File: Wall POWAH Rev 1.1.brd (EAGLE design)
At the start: 36.8 x 53.3 mm, 13 parts

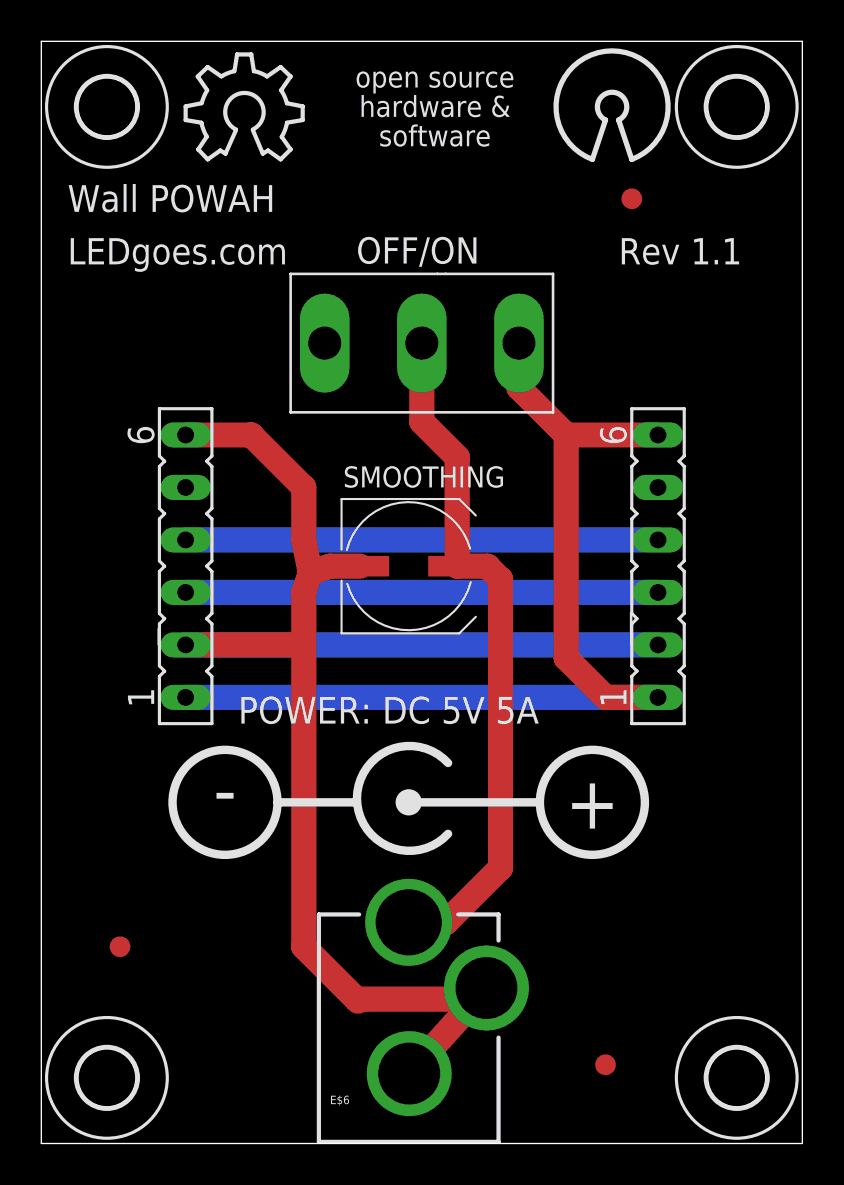
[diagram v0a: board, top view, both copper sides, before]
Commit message: Slight changes made to Rev 1 before production, including Power LED and polarity silkscreening
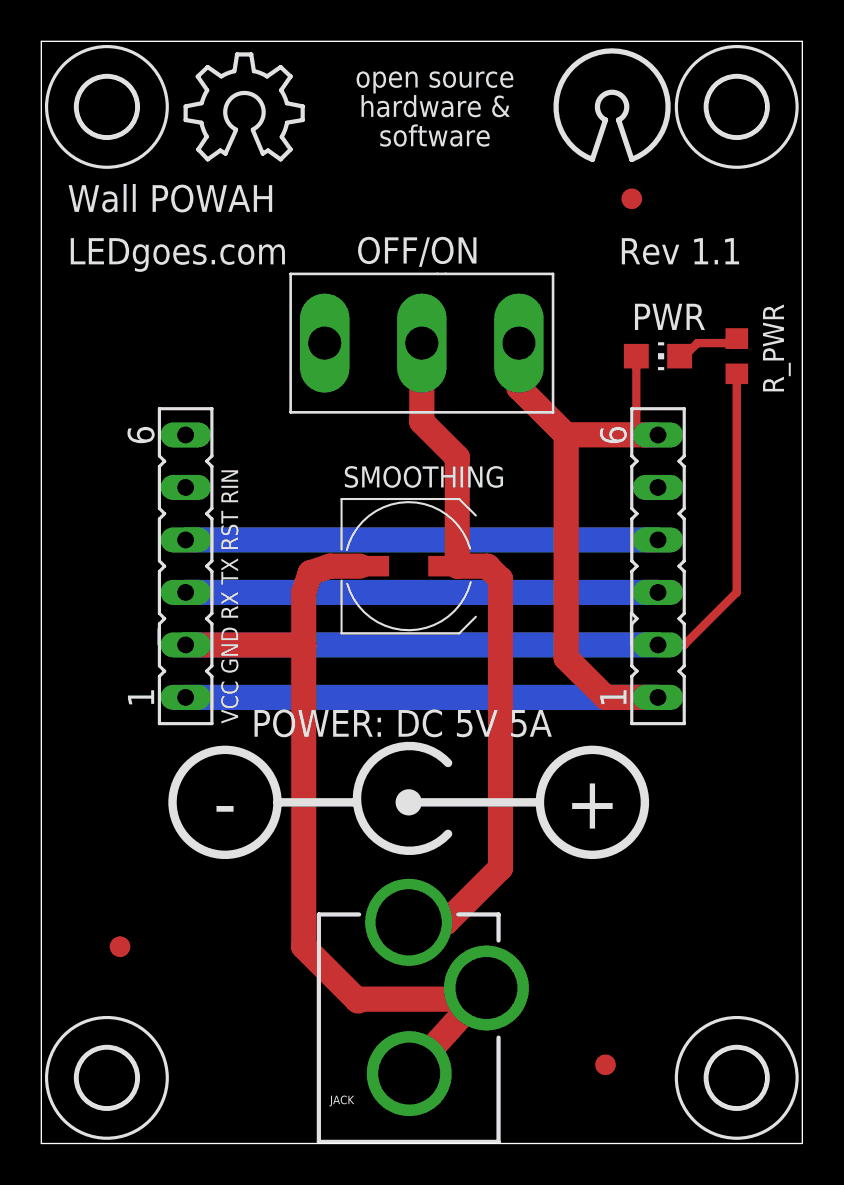
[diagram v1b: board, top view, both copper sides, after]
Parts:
- added PWR: (no value), led:CHIP-LED0805
- added R_PWR: (no value), eagle-ltspice:R0603
- renumbered E$6 to JACK
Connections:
- new net S$5: PWR.C, R_PWR.2
- net GND: now also R_PWR.1; no longer _.6
- net VCC: now also PWR.A
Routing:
- net GND: track 75.9 -> 80.5 mm
- net VCC: track 48.7 -> 52.7 mm
- net S$5: track 0.00 -> 3.11 mm
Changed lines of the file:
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@@
 <wire x1="43.18" y1="50.8" x2="6.35" y2="50.8" width="0" layer="20"/>
 <text x="7.62" y="40.005" size="1.27" layer="25" font="vector">LEDgoes.com</text>
-<text x="10.16" y="17.78" size="0.8128" layer="26" font="vector" rot="MR90">VCC GND RX TX RST RIN</text>
+<text x="15.875" y="17.78" size="0.8128" layer="25" font="vector" rot="R90">VCC GND RX TX RST RIN</text>
 <text x="25.4" y="45.72" size="1.016" layer="25" font="vector" distance="40" align="bottom-center">open source
 hardware &amp;
@@
 <text x="7.62" y="42.545" size="1.2954" layer="25" font="vector">Wall POWAH</text>
 <text x="34.29" y="40.005" size="1.27" layer="25" font="vector">Rev 1.1</text>
-<text x="15.875" y="17.78" size="1.2954" layer="25" font="vector">POWER: DC 5V 5A</text>
+<text x="16.51" y="17.145" size="1.2954" layer="25" font="vector">POWER: DC 5V 5A</text>
 <circle x="15.24" y="13.97" radius="2.54" width="0.4064" layer="25"/>
 <wire x1="26.035" y1="12.446" x2="26.035" y2="15.875" width="0.4064" layer="25" curve="-275"/>
@@
 <circle x="24.13" y="13.97" radius="0.635" width="0" layer="25"/>
 <wire x1="24.765" y1="13.97" x2="30.48" y2="13.97" width="0.4064" layer="25"/>
-<text x="15.24" y="13.335" size="2.54" layer="25" align="bottom-center">-</text>
-<text x="33.02" y="12.7" size="2.54" layer="25" align="bottom-center">+</text>
+<text x="15.24" y="12.7" size="2.54" layer="25" font="vector" align="bottom-center">-</text>
+<text x="33.02" y="12.7" size="2.54" layer="25" font="vector" align="bottom-center">+</text>
 </plain>
 <attributes>
@@
 <element name="E$2" library="holes" package="2,8" value="" x="40.005" y="47.625"/>
 <element name="E$5" library="holes" package="2,8" value="" x="40.005" y="0.635"/>
-<element name="E$6" library="SparkFun-Connectors" package="POWER_JACK_PTH_LOCK" value="" x="24.13" y="-5.715"/>
-<element name="SMOOTHING" library="rcl" package="UD-6,3X7,7_NICHICON" value="100uF" x="24.13" y="25.4"/>
+<element name="JACK" library="SparkFun-Connectors" package="POWER_JACK_PTH_LOCK" value="" x="24.13" y="-5.715"/>
+<element name="SMOOTHING" library="rcl" package="UD-6,3X7,7_NICHICON" value="100uF" x="24.13" y="25.4" smashed="yes">
+<attribute name="NAME" x="20.955" y="29.21" size="1.016" layer="25" font="vector"/>
+<attribute name="VALUE" x="20.955" y="20.955" size="1.016" layer="27" font="vector"/>
+</element>
 <element name="OFF/ON" library="LEDgoes" package="SPDT-5A" value=" " x="24.765" y="36.195" smashed="yes">
-<attribute name="NAME" x="21.59" y="40.045" size="1.27" layer="25"/>
+<attribute name="NAME" x="21.59" y="40.045" size="1.27" layer="25" font="vector"/>
 </element>
 <element name="E$7" library="adafruit" package="FIDUCIAL_1MM" value="" x="34.925" y="43.18"/>
 <element name="E$8" library="adafruit" package="FIDUCIAL_1MM" value="" x="33.655" y="1.27"/>
 <element name="E$9" library="adafruit" package="FIDUCIAL_1MM" value="" x="10.16" y="6.985"/>
+<element name="PWR" library="led" package="CHIP-LED0805" value="" x="36.195" y="35.56" smashed="yes" rot="R270">
+<attribute name="NAME" x="34.925" y="36.83" size="1.27" layer="25" font="vector"/>
+<attribute name="VALUE" x="34.925" y="33.02" size="1.27" layer="27"/>
+</element>
+<element name="R_PWR" library="eagle-ltspice" package="R0603" value="" x="40.005" y="35.56" smashed="yes" rot="R90">
+<attribute name="NAME" x="41.275" y="38.1" size="1.016" layer="25" font="vector" rot="R270"/>
+<attribute name="VALUE" x="41.91" y="34.925" size="1.27" layer="27" rot="R90"/>
+</element>
 </elements>
 <signals>
@@
 <wire x1="19.3675" y1="25.0825" x2="20.32" y2="25.4" width="1.2192" layer="1"/>
 <wire x1="20.32" y1="25.4" x2="21.78" y2="25.4" width="1.2192" layer="1"/>
-<contactref element="E$6" pad="GNDBREAK"/>
-<contactref element="E$6" pad="GND"/>
+<contactref element="JACK" pad="GNDBREAK"/>
+<contactref element="JACK" pad="GND"/>
 <wire x1="24.1554" y1="0.842" x2="27.8916" y2="4.985" width="1.2192" layer="1"/>
 <wire x1="27.8916" y1="4.985" x2="27.845" y2="4.985" width="1.2192" layer="1"/>
 <wire x1="27.845" y1="4.985" x2="27.305" y2="4.445" width="1.2192" layer="1"/>
 <wire x1="27.305" y1="4.445" x2="21.59" y2="4.445" width="1.2192" layer="1"/>
-<contactref element="_" pad="6"/>
-<wire x1="13.335" y1="31.75" x2="16.51" y2="31.75" width="1.2192" layer="1"/>
-<wire x1="16.51" y1="31.75" x2="19.05" y2="29.21" width="1.2192" layer="1"/>
-<wire x1="19.05" y1="29.21" x2="19.05" y2="26.67" width="1.2192" layer="1"/>
-<wire x1="19.05" y1="26.67" x2="19.3675" y2="25.0825" width="1.2192" layer="1"/>
+<contactref element="R_PWR" pad="1"/>
+<wire x1="40.005" y1="34.71" x2="40.005" y2="24.13" width="0.4064" layer="1"/>
+<wire x1="40.005" y1="24.13" x2="37.465" y2="21.59" width="0.4064" layer="1"/>
+<wire x1="37.465" y1="21.59" x2="36.195" y2="21.59" width="0.4064" layer="1"/>
 </signal>
 <signal name="VCC">
@@
 <wire x1="29.465" y1="36.195" x2="29.465" y2="34.035" width="1.2192" layer="1"/>
 <wire x1="29.465" y1="34.035" x2="31.75" y2="31.75" width="1.2192" layer="1"/>
-<wire x1="31.75" y1="31.75" x2="36.195" y2="31.75" width="1.2192" layer="1"/>
+<wire x1="31.75" y1="31.75" x2="35.56" y2="31.75" width="1.2192" layer="1"/>
+<wire x1="35.56" y1="31.75" x2="36.195" y2="31.75" width="1.2192" layer="1"/>
 <wire x1="36.195" y1="19.05" x2="33.655" y2="19.05" width="1.2192" layer="1"/>
 <wire x1="33.655" y1="19.05" x2="31.75" y2="20.955" width="1.2192" layer="1"/>
 <wire x1="31.75" y1="20.955" x2="31.75" y2="31.75" width="1.2192" layer="1"/>
+<contactref element="PWR" pad="A"/>
+<wire x1="35.145" y1="35.56" x2="35.145" y2="32.165" width="0.4064" layer="1"/>
+<wire x1="35.145" y1="32.165" x2="35.56" y2="31.75" width="0.4064" layer="1"/>
 </signal>
 <signal name="S$1">
 <contactref element="SMOOTHING" pad="+"/>
-<contactref element="E$6" pad="PWR"/>
+<contactref element="JACK" pad="PWR"/>
 <wire x1="24.13" y1="8.1628" x2="25.9428" y2="8.1628" width="1.2192" layer="1"/>
 <wire x1="25.9428" y1="8.1628" x2="28.575" y2="10.795" width="1.2192" layer="1"/>
@@
 <wire x1="36.195" y1="26.67" x2="13.335" y2="26.67" width="1.2192" layer="16"/>
 </signal>
+<signal name="S$5">
+<contactref element="R_PWR" pad="2"/>
+<contactref element="PWR" pad="C"/>
+<wire x1="37.245" y1="35.56" x2="37.465" y2="35.56" width="0.4064" layer="1"/>
+<wire x1="37.465" y1="35.56" x2="38.1" y2="36.195" width="0.4064" layer="1"/>
+<wire x1="38.1" y1="36.195" x2="39.79" y2="36.195" width="0.4064" layer="1"/>
+<wire x1="39.79" y1="36.195" x2="40.005" y2="36.41" width="0.4064" layer="1"/>
+</signal>
 </signals>
